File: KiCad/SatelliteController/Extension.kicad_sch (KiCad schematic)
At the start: 2 parts, among them J7 CONN_STATUS_PANEL, J8 CONN_PANEL_BAORD_2

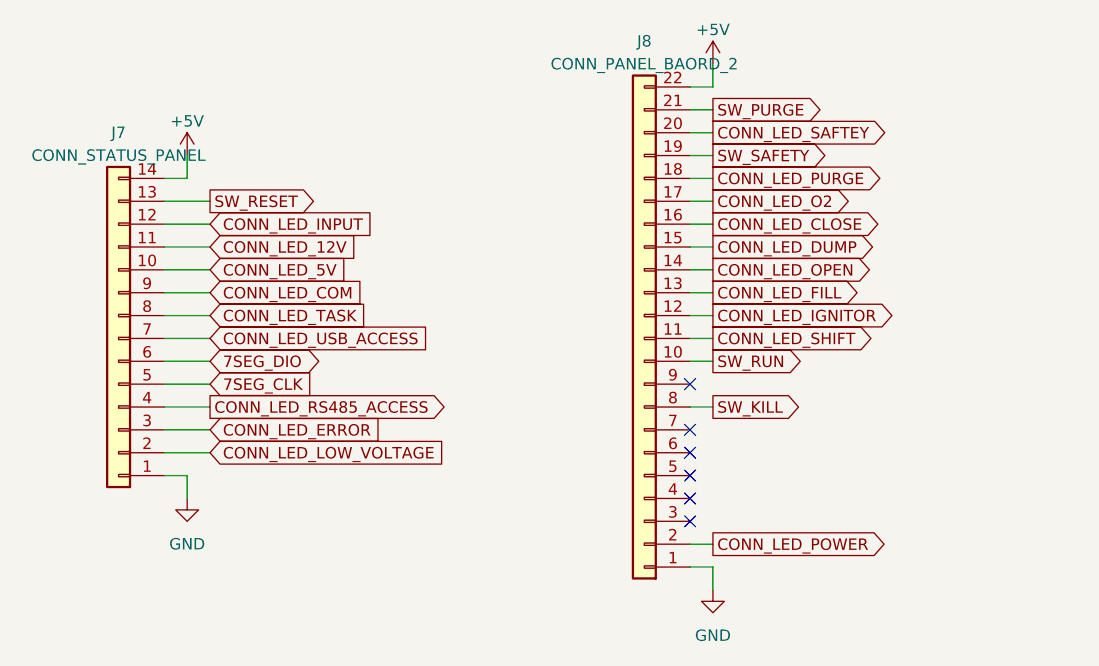
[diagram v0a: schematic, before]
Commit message: サテコンの制御スイッチをプルダウンに変更
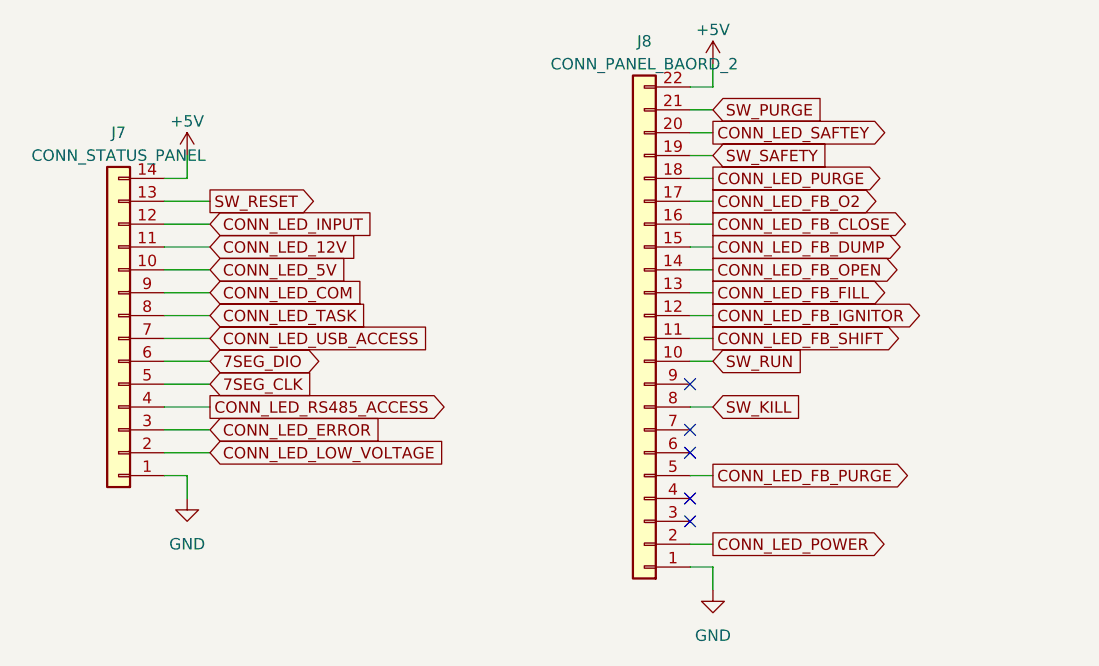
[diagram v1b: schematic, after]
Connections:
- net CONN_LED_FB_PURGE: now reaches J8.5 (Pin_5)
- net CONN_LED_CLOSE renamed CONN_LED_FB_CLOSE
- net CONN_LED_DUMP renamed CONN_LED_FB_DUMP
- net CONN_LED_FILL renamed CONN_LED_FB_FILL
- net CONN_LED_IGNITOR renamed CONN_LED_FB_IGNITOR
- net CONN_LED_O2 renamed CONN_LED_FB_O2
- net CONN_LED_OPEN renamed CONN_LED_FB_OPEN
- net CONN_LED_SHIFT renamed CONN_LED_FB_SHIFT
- no-connect marks 6 -> 5
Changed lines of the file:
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@@
   (no_connect (at 91.44 71.12))
   (no_connect (at 91.44 81.28))
-  (no_connect (at 91.44 76.2))
   (no_connect (at 91.44 73.66))
   (wire (pts (xy 91.44 45.72) (xy 93.98 45.72))
@@
     (stroke (width 0) (type default))
   )
+  (wire (pts (xy 91.44 76.2) (xy 93.98 76.2))
+    (stroke (width 0) (type default))
+  )
   (wire (pts (xy 91.44 38.1) (xy 93.98 38.1))
     (stroke (width 0) (type default))
@@
     (stroke (width 0) (type default))
   )
-  (global_label "CONN_LED_DUMP" (shape output) (at 93.98 50.8 0) (fields_autoplaced)
-    (effects (font (size 1.27 1.27)) (justify left))
-    (property "Intersheetrefs" "${INTERSHEET_REFS}" (at 112.8515 50.8 0)
+  (global_label "CONN_LED_FB_DUMP" (shape output) (at 93.98 50.8 0) (fields_autoplaced)
+    (effects (font (size 1.27 1.27)) (justify left))
+    (property "Intersheetrefs" "${INTERSHEET_REFS}" (at 116.1777 50.8 0)
       (effects (font (size 1.27 1.27)) (justify left) hide)
     )
@@
     )
   )
-  (global_label "SW_KILL" (shape output) (at 93.98 68.58 0) (fields_autoplaced)
+  (global_label "SW_KILL" (shape input) (at 93.98 68.58 0) (fields_autoplaced)
     (effects (font (size 1.27 1.27)) (justify left))
     (property "Intersheetrefs" "${INTERSHEET_REFS}" (at 104.4453 68.58 0)
@@
     )
   )
-  (global_label "SW_PURGE" (shape output) (at 93.98 35.56 0) (fields_autoplaced)
+  (global_label "SW_PURGE" (shape input) (at 93.98 35.56 0) (fields_autoplaced)
     (effects (font (size 1.27 1.27)) (justify left))
     (property "Intersheetrefs" "${INTERSHEET_REFS}" (at 106.8038 35.56 0)
@@
     )
   )
-  (global_label "CONN_LED_OPEN" (shape output) (at 93.98 53.34 0) (fields_autoplaced)
-    (effects (font (size 1.27 1.27)) (justify left))
-    (property "Intersheetrefs" "${INTERSHEET_REFS}" (at 112.6096 53.34 0)
+  (global_label "CONN_LED_FB_OPEN" (shape output) (at 93.98 53.34 0) (fields_autoplaced)
+    (effects (font (size 1.27 1.27)) (justify left))
+    (property "Intersheetrefs" "${INTERSHEET_REFS}" (at 115.9358 53.34 0)
       (effects (font (size 1.27 1.27)) (justify left) hide)
     )
@@
     )
   )
-  (global_label "CONN_LED_SHIFT" (shape output) (at 93.98 60.96 0) (fields_autoplaced)
-    (effects (font (size 1.27 1.27)) (justify left))
-    (property "Intersheetrefs" "${INTERSHEET_REFS}" (at 112.7306 60.96 0)
-      (effects (font (size 1.27 1.27)) (justify left) hide)
-    )
-  )
-  (global_label "CONN_LED_FILL" (shape output) (at 93.98 55.88 0) (fields_autoplaced)
-    (effects (font (size 1.27 1.27)) (justify left))
-    (property "Intersheetrefs" "${INTERSHEET_REFS}" (at 111.2792 55.88 0)
-      (effects (font (size 1.27 1.27)) (justify left) hide)
-    )
-  )
-  (global_label "CONN_LED_O2" (shape output) (at 93.98 45.72 0) (fields_autoplaced)
-    (effects (font (size 1.27 1.27)) (justify left))
-    (property "Intersheetrefs" "${INTERSHEET_REFS}" (at 110.0696 45.72 0)
+  (global_label "CONN_LED_FB_SHIFT" (shape output) (at 93.98 60.96 0) (fields_autoplaced)
+    (effects (font (size 1.27 1.27)) (justify left))
+    (property "Intersheetrefs" "${INTERSHEET_REFS}" (at 116.0568 60.96 0)
+      (effects (font (size 1.27 1.27)) (justify left) hide)
+    )
+  )
+  (global_label "CONN_LED_FB_FILL" (shape output) (at 93.98 55.88 0) (fields_autoplaced)
+    (effects (font (size 1.27 1.27)) (justify left))
+    (property "Intersheetrefs" "${INTERSHEET_REFS}" (at 114.6054 55.88 0)
+      (effects (font (size 1.27 1.27)) (justify left) hide)
+    )
+  )
+  (global_label "CONN_LED_FB_O2" (shape output) (at 93.98 45.72 0) (fields_autoplaced)
+    (effects (font (size 1.27 1.27)) (justify left))
+    (property "Intersheetrefs" "${INTERSHEET_REFS}" (at 113.3958 45.72 0)
       (effects (font (size 1.27 1.27)) (justify left) hide)
     )
@@
     )
   )
-  (global_label "SW_RUN" (shape output) (at 93.98 63.5 0) (fields_autoplaced)
+  (global_label "SW_RUN" (shape input) (at 93.98 63.5 0) (fields_autoplaced)
     (effects (font (size 1.27 1.27)) (justify left))
     (property "Intersheetrefs" "${INTERSHEET_REFS}" (at 104.4453 63.5 0)
@@
     )
   )
-  (global_label "SW_SAFETY" (shape output) (at 93.98 40.64 0) (fields_autoplaced)
+  (global_label "SW_SAFETY" (shape input) (at 93.98 40.64 0) (fields_autoplaced)
     (effects (font (size 1.27 1.27)) (justify left))
     (property "Intersheetrefs" "${INTERSHEET_REFS}" (at 107.1062 40.64 0)
@@
     )
   )
-  (global_label "CONN_LED_IGNITOR" (shape output) (at 93.98 58.42 0) (fields_autoplaced)
-    (effects (font (size 1.27 1.27)) (justify left))
-    (property "Intersheetrefs" "${INTERSHEET_REFS}" (at 114.9078 58.42 0)
+  (global_label "CONN_LED_FB_IGNITOR" (shape output) (at 93.98 58.42 0) (fields_autoplaced)
+    (effects (font (size 1.27 1.27)) (justify left))
+    (property "Intersheetrefs" "${INTERSHEET_REFS}" (at 118.234 58.42 0)
+      (effects (font (size 1.27 1.27)) (justify left) hide)
+    )
+  )
+  (global_label "CONN_LED_FB_PURGE" (shape output) (at 93.98 76.2 0) (fields_autoplaced)
+    (effects (font (size 1.27 1.27)) (justify left))
+    (property "Intersheetrefs" "${INTERSHEET_REFS}" (at 117.1453 76.2 0)
       (effects (font (size 1.27 1.27)) (justify left) hide)
     )
@@
     )
   )
-  (global_label "CONN_LED_CLOSE" (shape output) (at 93.98 48.26 0) (fields_autoplaced)
-    (effects (font (size 1.27 1.27)) (justify left))
-    (property "Intersheetrefs" "${INTERSHEET_REFS}" (at 113.5167 48.26 0)
-      (effects (font (size 1.27 1.27)) (justify left) hide)
-    )
+  (global_label "CONN_LED_FB_CLOSE" (shape output) (at 93.98 48.26 0) (fields_autoplaced)
+    (effects (font (size 1.27 1.27)) (justify left))
+    (property "Intersheetrefs" "${INTERSHEET_REFS}" (at 116.8429 48.26 0)
+      (effects (font (size 1.27 1.27)) (justify left) hide)
+    )

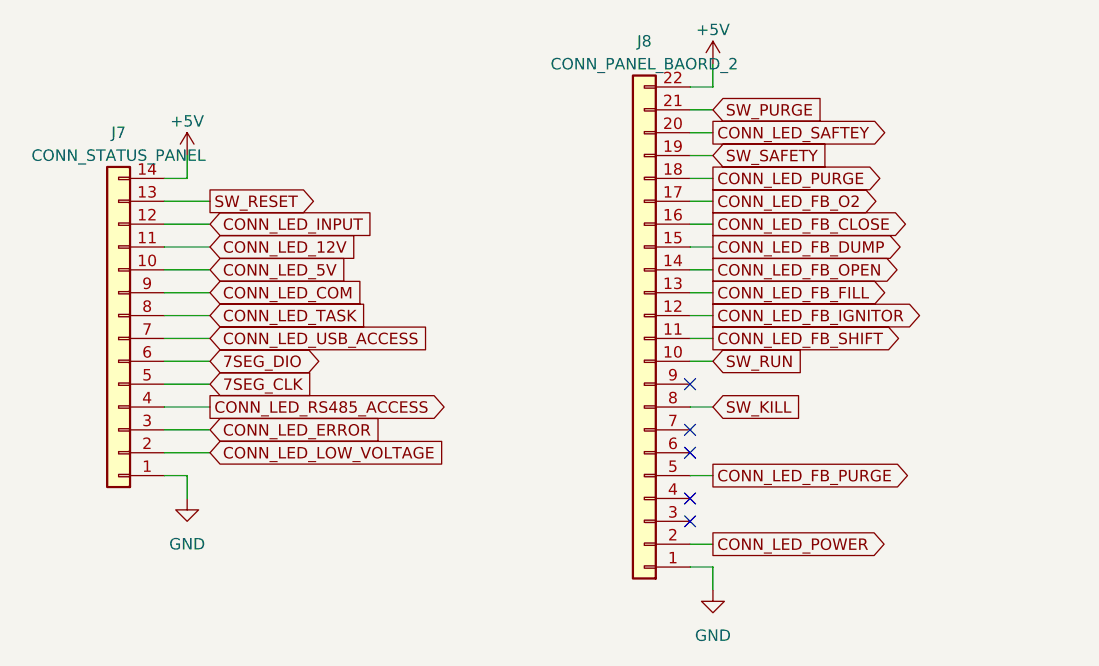
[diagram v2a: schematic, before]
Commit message: 電磁弁制御回路を整理
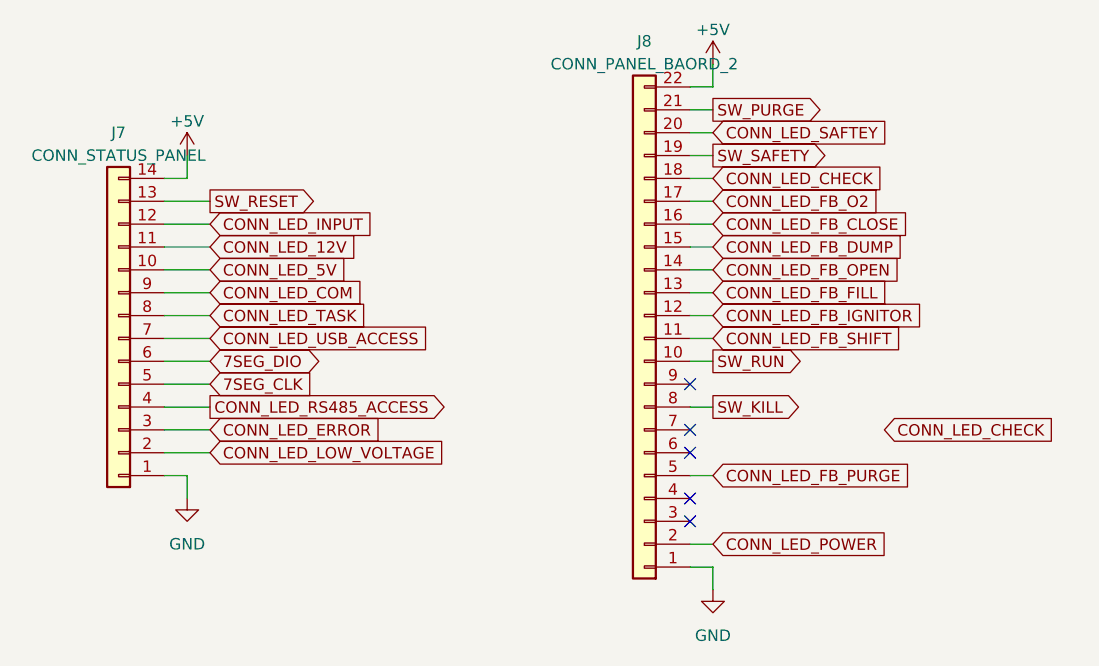
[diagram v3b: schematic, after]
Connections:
- net CONN_LED_PURGE renamed CONN_LED_CHECK

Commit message: 配線
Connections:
- net SW_PURGE renamed SW_CHECK
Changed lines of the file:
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@@
-		)
-	)
-	(global_label "CONN_LED_CHECK"
-		(shape input)
-		(at 113.03 71.12 0)
-		(fields_autoplaced yes)
-		(effects
-			(font
-				(size 1.27 1.27)
-			)
-			(justify left)
-		)
-		(property "Intersheetrefs" "${INTERSHEET_REFS}"
-			(at 132.9485 71.12 0)
-			(effects
-				(font
-					(size 1.27 1.27)
-				)
-				(justify left)
-				(hide yes)
-			)
-		)
-	)
-	(global_label "SW_PURGE"
-		(shape output)
-		(at 93.98 35.56 0)
-		(fields_autoplaced yes)
-		(effects
-			(font
-				(size 1.27 1.27)
-			)
-			(justify left)
-		)
-		(property "Intersheetrefs" "${INTERSHEET_REFS}"
-			(at 106.8832 35.56 0)
-			(effects
-				(font
-					(size 1.27 1.27)
-				)
-				(justify left)
-				(hide yes)
-			)
 		)
 	)
@@
 			(effects
 				(font
+					(size 1.27 1.27)
+				)
+				(justify left)
+				(hide yes)
+			)
+		)
+	)
+	(global_label "SW_CHECK"
+		(shape output)
+		(at 93.98 35.56 0)
+		(fields_autoplaced yes)
+		(effects
+			(font
+				(size 1.27 1.27)
+			)
+			(justify left)
+		)
+		(property "Intersheetrefs" "${INTERSHEET_REFS}"
+			(at 106.8832 35.56 0)
+			(effects
+				(font
